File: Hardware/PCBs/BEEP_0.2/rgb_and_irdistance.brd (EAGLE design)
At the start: 22.2 x 13.3 mm, 5 parts, among them X1 MICROMATCH-8

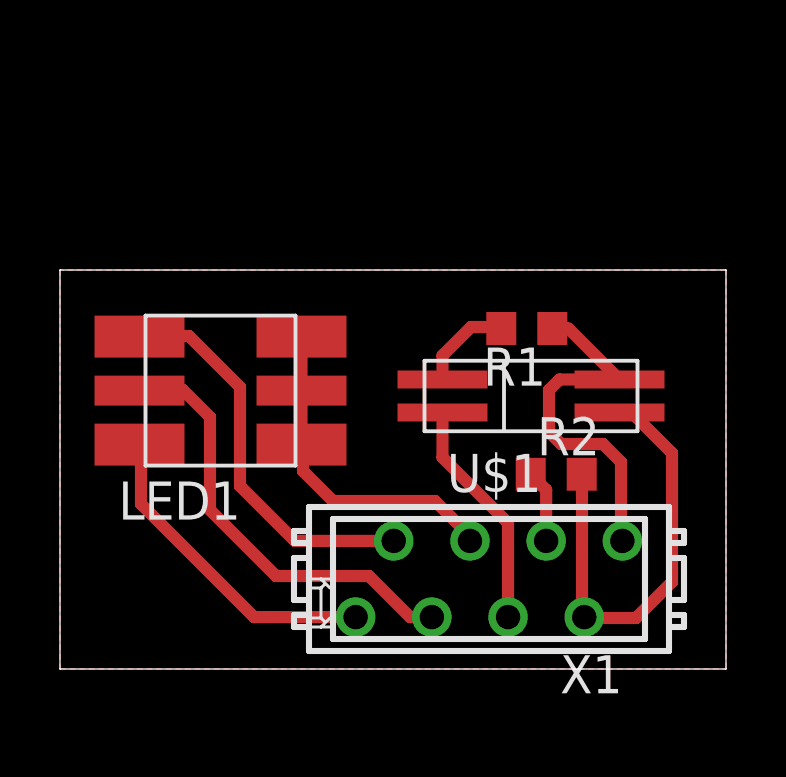
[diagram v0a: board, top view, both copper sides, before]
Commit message: enhance routing fix rgb and ir distance board (connector was on the wrong side)
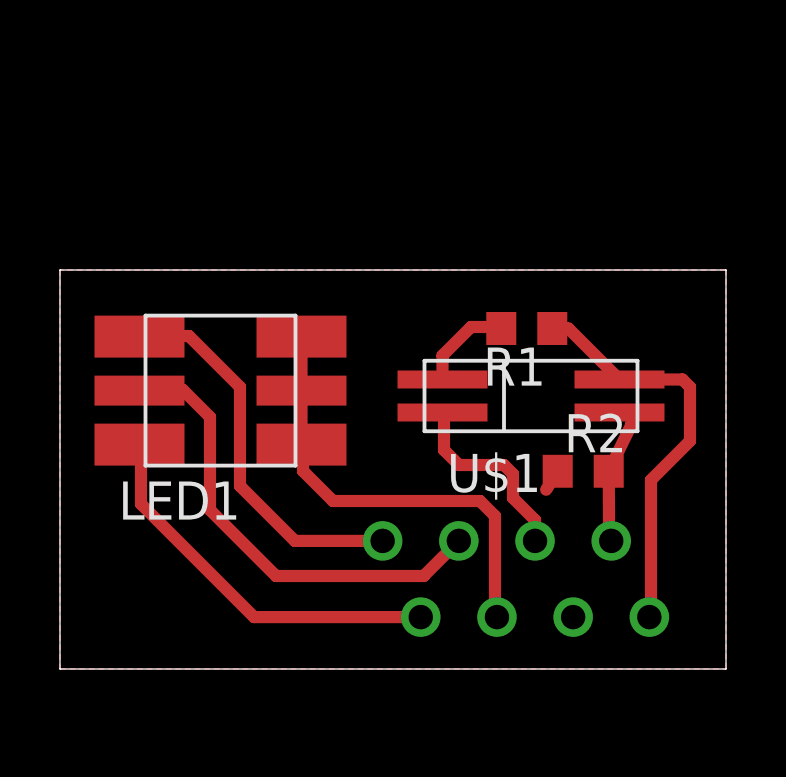
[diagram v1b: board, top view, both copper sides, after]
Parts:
- moved R2 0.91 mm to (17.4, 6.59)
- moved X1 0.90 mm to (15.2, 3.00), flipped to the bottom, turned to 0 degrees
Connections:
- net RGB_ANODE_1: now also LED1.R1; no longer LED1.B1
- net RGB_ANODE_3: now also LED1.B1; no longer LED1.R1
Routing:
- net ADISTANCE: track 14.9 -> 4.89 mm
- net RGB_COMMON_K: track 11.1 -> 14.9 mm
- net RGB_ANODE_1: track 10.8 -> 12.9 mm
- net GND: track 2.43 -> 0.73 mm
- net IR_LED_K: track 8.70 -> 7.41 mm
- net +5V: track 12.4 -> 13.6 mm
- net RGB_ANODE_2: track 14.7 -> 15.5 mm
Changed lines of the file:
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@@
 <element name="LED1" library="BEEP" package="5050LED" value="F503605050" x="5.35" y="9.28"/>
 <element name="R1" library="rcl" package="R0603" value="" x="15.56" y="11.35" rot="R180"/>
-<element name="R2" library="rcl" package="R0603" value="" x="16.54" y="6.49"/>
-<element name="X1" library="con-amp-micromatch" package="MICROMATCH-8" value="MICROMATCH-8" x="14.3" y="3" rot="R180">
-<attribute name="OC_NEWARK" value="26H0301" x="14.3" y="3" size="1.778" layer="27" rot="R180" display="off"/>
-<attribute name="MPN" value="7-215464-8" x="14.3" y="3" size="1.778" layer="27" rot="R180" display="off"/>
-<attribute name="MF" value="FARNELL" x="14.3" y="3" size="1.778" layer="27" rot="R180" display="off"/>
-<attribute name="OC_FARNELL" value="3784642" x="14.3" y="3" size="1.778" layer="27" rot="R180" display="off"/>
+<element name="R2" library="rcl" package="R0603" value="" x="17.44" y="6.59"/>
+<element name="X1" library="con-amp-micromatch" package="MICROMATCH-8" value="MICROMATCH-8" x="15.2" y="3" rot="MR0">
+<attribute name="OC_NEWARK" value="26H0301" x="15.2" y="3" size="1.778" layer="28" rot="MR0" display="off"/>
+<attribute name="MPN" value="7-215464-8" x="15.2" y="3" size="1.778" layer="28" rot="MR0" display="off"/>
+<attribute name="MF" value="FARNELL" x="15.2" y="3" size="1.778" layer="28" rot="MR0" display="off"/>
+<attribute name="OC_FARNELL" value="3784642" x="15.2" y="3" size="1.778" layer="28" rot="MR0" display="off"/>
 </element>
 <element name="U$1" library="BEEP" package="HSDL-9100" value="HSDL-9100" x="15.7" y="9.1"/>
@@
 <wire x1="8.05" y1="7.48" x2="8.05" y2="9.28" width="0.4064" layer="1"/>
 <wire x1="8.05" y1="9.28" x2="8.05" y2="11.08" width="0.4064" layer="1"/>
-<wire x1="13.665" y1="4.27" x2="13.665" y2="4.435" width="0.4064" layer="1"/>
-<wire x1="13.665" y1="4.435" x2="12.5" y2="5.6" width="0.4064" layer="1"/>
-<wire x1="12.5" y1="5.6" x2="9.1" y2="5.6" width="0.4064" layer="1"/>
 <wire x1="9.1" y1="5.6" x2="8.1" y2="6.6" width="0.4064" layer="1"/>
+<wire x1="9.1" y1="5.6" x2="14" y2="5.6" width="0.4064" layer="1"/>
+<wire x1="14" y1="5.6" x2="14.5" y2="5.1" width="0.4064" layer="1"/>
+<wire x1="14.5" y1="5.1" x2="14.5" y2="1.795" width="0.4064" layer="1"/>
+<wire x1="14.5" y1="1.795" x2="14.565" y2="1.73" width="0.4064" layer="1"/>
 </signal>
 <signal name="ADISTANCE">
@@
 <contactref element="U$1" pad="DET_A"/>
 <wire x1="18.65" y1="8.55" x2="19.05" y2="8.55" width="0.4064" layer="1"/>
-<wire x1="19.05" y1="8.55" x2="20.4" y2="7.2" width="0.4064" layer="1"/>
-<wire x1="20.4" y1="7.2" x2="20.4" y2="2.9" width="0.4064" layer="1"/>
-<wire x1="20.4" y1="2.9" x2="19.2" y2="1.7" width="0.4064" layer="1"/>
-<wire x1="19.2" y1="1.7" x2="17.545" y2="1.7" width="0.4064" layer="1"/>
-<wire x1="17.545" y1="1.7" x2="17.475" y2="1.73" width="0.4064" layer="1"/>
-<wire x1="17.4" y1="6.18" x2="17.4" y2="1.705" width="0.4064" layer="1"/>
-<wire x1="17.4" y1="1.705" x2="17.475" y2="1.73" width="0.4064" layer="1"/>
-<wire x1="17.4" y1="6.18" x2="17.39" y2="6.49" width="0.4064" layer="1"/>
+<wire x1="18.3" y1="5.28" x2="18.29" y2="6.59" width="0.4064" layer="1"/>
+<wire x1="18.3" y1="5.28" x2="18.3" y2="4.345" width="0.4064" layer="1"/>
+<wire x1="18.3" y1="4.345" x2="18.375" y2="4.27" width="0.4064" layer="1"/>
+<wire x1="19.05" y1="8.55" x2="19.05" y2="8.15" width="0.4064" layer="1"/>
+<wire x1="19.05" y1="8.15" x2="18.29" y2="6.59" width="0.4064" layer="1"/>
 </signal>
 <signal name="N$2">
@@
 </signal>
 <signal name="RGB_ANODE_1">
-<contactref element="LED1" pad="B1"/>
 <contactref element="X1" pad="1"/>
-<wire x1="2.6" y1="7.43" x2="2.65" y2="7.48" width="0.4064" layer="1"/>
-<wire x1="9.855" y1="1.73" x2="6.47" y2="1.73" width="0.4064" layer="1"/>
-<wire x1="6.47" y1="1.73" x2="2.7" y2="5.5" width="0.4064" layer="1"/>
-<wire x1="2.7" y1="5.5" x2="2.7" y2="7.43" width="0.4064" layer="1"/>
-<wire x1="2.7" y1="7.43" x2="2.65" y2="7.48" width="0.4064" layer="1"/>
+<contactref element="LED1" pad="R1"/>
+<wire x1="6" y1="9.4" x2="4.3" y2="11.1" width="0.4064" layer="1"/>
+<wire x1="4.3" y1="11.1" x2="2.67" y2="11.1" width="0.4064" layer="1"/>
+<wire x1="2.67" y1="11.1" x2="2.65" y2="11.08" width="0.4064" layer="1"/>
+<wire x1="7.83" y1="4.27" x2="6" y2="6.1" width="0.4064" layer="1"/>
+<wire x1="6" y1="6.1" x2="6" y2="9.4" width="0.4064" layer="1"/>
+<wire x1="7.83" y1="4.27" x2="10.755" y2="4.27" width="0.4064" layer="1"/>
 </signal>
 <signal name="RGB_ANODE_2">
@@
 <wire x1="2.67" y1="9.3" x2="2.65" y2="9.28" width="0.4064" layer="1"/>
 <contactref element="X1" pad="3"/>
-<wire x1="12.395" y1="1.73" x2="11.67" y2="1.73" width="0.4064" layer="1"/>
-<wire x1="11.67" y1="1.73" x2="10.3" y2="3.1" width="0.4064" layer="1"/>
-<wire x1="10.3" y1="3.1" x2="7.2" y2="3.1" width="0.4064" layer="1"/>
 <wire x1="7.2" y1="3.1" x2="5" y2="5.3" width="0.4064" layer="1"/>
+<wire x1="7.2" y1="3.1" x2="12.125" y2="3.1" width="0.4064" layer="1"/>
+<wire x1="12.125" y1="3.1" x2="13.295" y2="4.27" width="0.4064" layer="1"/>
 </signal>
 <signal name="RGB_ANODE_3">
-<contactref element="LED1" pad="R1"/>
-<wire x1="6" y1="9.4" x2="4.3" y2="11.1" width="0.4064" layer="1"/>
-<wire x1="4.3" y1="11.1" x2="2.67" y2="11.1" width="0.4064" layer="1"/>
-<wire x1="2.67" y1="11.1" x2="2.65" y2="11.08" width="0.4064" layer="1"/>
 <contactref element="X1" pad="2"/>
-<wire x1="11.125" y1="4.27" x2="7.83" y2="4.27" width="0.4064" layer="1"/>
-<wire x1="7.83" y1="4.27" x2="6" y2="6.1" width="0.4064" layer="1"/>
-<wire x1="6" y1="6.1" x2="6" y2="9.4" width="0.4064" layer="1"/>
+<contactref element="LED1" pad="B1"/>
+<wire x1="2.6" y1="7.43" x2="2.65" y2="7.48" width="0.4064" layer="1"/>
+<wire x1="6.47" y1="1.73" x2="2.7" y2="5.5" width="0.4064" layer="1"/>
+<wire x1="2.7" y1="5.5" x2="2.7" y2="7.43" width="0.4064" layer="1"/>
+<wire x1="2.7" y1="7.43" x2="2.65" y2="7.48" width="0.4064" layer="1"/>
+<wire x1="6.47" y1="1.73" x2="12.025" y2="1.73" width="0.4064" layer="1"/>
 </signal>
 <signal name="IR_LED_K">
 <contactref element="U$1" pad="LED_K"/>
 <contactref element="X1" pad="5"/>
-<wire x1="14.935" y1="1.73" x2="14.935" y2="4.865" width="0.4064" layer="1"/>
 <wire x1="11.8" y1="8.5" x2="12.7" y2="8.5" width="0.4064" layer="1"/>
 <wire x1="12.7" y1="8.5" x2="12.75" y2="8.55" width="0.4064" layer="1"/>
-<wire x1="14.935" y1="4.865" x2="12.75" y2="7.05" width="0.4064" layer="1"/>
-<wire x1="12.75" y1="8.55" x2="12.75" y2="7.05" width="0.4064" layer="1"/>
+<wire x1="15.835" y1="4.27" x2="15.835" y2="4.965" width="0.4064" layer="1"/>
+<wire x1="15.835" y1="4.965" x2="15.1" y2="5.7" width="0.4064" layer="1"/>
+<wire x1="15.1" y1="5.7" x2="15.1" y2="6.5" width="0.4064" layer="1"/>
+<wire x1="15.1" y1="6.5" x2="14.8" y2="6.8" width="0.4064" layer="1"/>
+<wire x1="14.8" y1="6.8" x2="13.3" y2="6.8" width="0.4064" layer="1"/>
+<wire x1="13.3" y1="6.8" x2="12.8" y2="7.3" width="0.4064" layer="1"/>
+<wire x1="12.8" y1="7.3" x2="12.8" y2="8.5" width="0.4064" layer="1"/>
+<wire x1="12.8" y1="8.5" x2="12.75" y2="8.55" width="0.4064" layer="1"/>
 </signal>
 <signal name="+5V">
@@
 <wire x1="16.41" y1="11.35" x2="16.95" y2="11.35" width="0.4064" layer="1"/>
 <wire x1="16.95" y1="11.35" x2="18.65" y2="9.65" width="0.4064" layer="1"/>
-<wire x1="18.65" y1="9.65" x2="16.65" y2="9.65" width="0.4064" layer="1"/>
-<wire x1="16.65" y1="9.65" x2="16.3" y2="9.3" width="0.4064" layer="1"/>
-<wire x1="16.3" y1="9.3" x2="16.3" y2="7.9" width="0.4064" layer="1"/>
-<wire x1="16.3" y1="7.9" x2="16.7" y2="7.5" width="0.4064" layer="1"/>
-<wire x1="16.7" y1="7.5" x2="18.1" y2="7.5" width="0.4064" layer="1"/>
-<wire x1="18.1" y1="7.5" x2="18.7" y2="6.9" width="0.4064" layer="1"/>
-<wire x1="18.7" y1="6.9" x2="18.7" y2="4.215" width="0.4064" layer="1"/>
-<wire x1="18.7" y1="4.215" x2="18.745" y2="4.27" width="0.4064" layer="1"/>
+<wire x1="18.65" y1="9.65" x2="20.75" y2="9.65" width="0.4064" layer="1"/>
+<wire x1="20.75" y1="9.65" x2="21" y2="9.4" width="0.4064" layer="1"/>
+<wire x1="21" y1="9.4" x2="21" y2="7.6" width="0.4064" layer="1"/>
+<wire x1="21" y1="7.6" x2="19.7" y2="6.3" width="0.4064" layer="1"/>
+<wire x1="19.7" y1="6.3" x2="19.7" y2="1.785" width="0.4064" layer="1"/>
+<wire x1="19.7" y1="1.785" x2="19.645" y2="1.73" width="0.4064" layer="1"/>
 </signal>
 <signal name="GND">
@@
 <vertex x="0" y="13.3"/>
 </polygon>
-<wire x1="16.205" y1="4.27" x2="16.205" y2="5.975" width="0.4064" layer="1"/>
-<wire x1="16.205" y1="5.975" x2="15.69" y2="6.49" width="0.4064" layer="1"/>
+<wire x1="16.205" y1="5.975" x2="16.59" y2="6.59" width="0.4064" layer="1"/>
 </signal>
 </signals>

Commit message: rearrange connectors routing
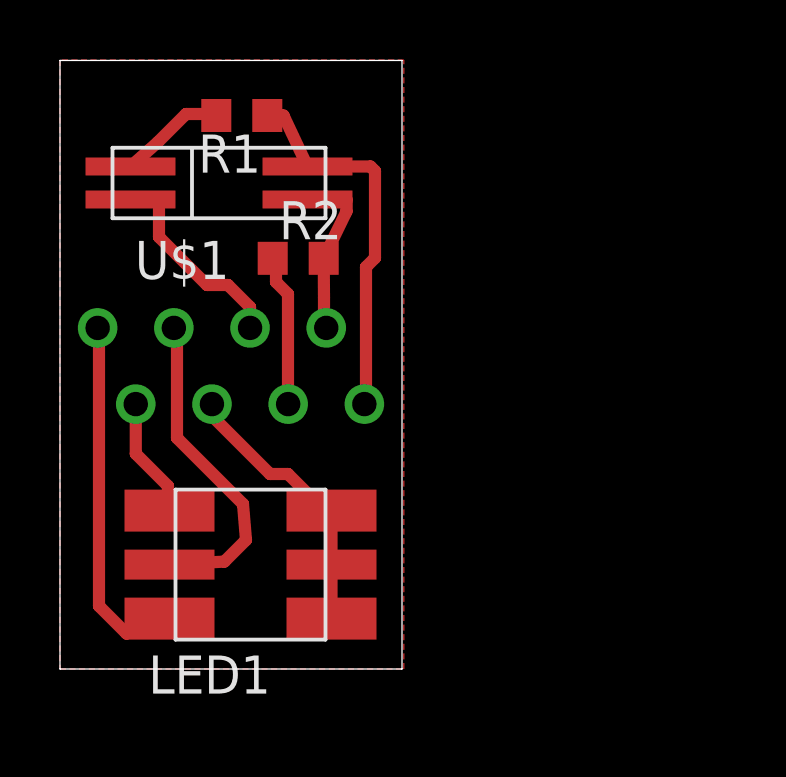
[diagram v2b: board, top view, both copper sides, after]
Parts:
- moved U$1 12.6 mm to (5.30, 16.2)
- moved R1 11.9 mm to (6.06, 18.4)
- moved R2 11.9 mm to (7.94, 13.7)
- moved X1 11.9 mm to (5.70, 10.1)
- moved LED1 5.89 mm to (6.35, 3.48)
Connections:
- net RGB_ANODE_1: now also LED1.B1; no longer LED1.R1
- net RGB_ANODE_3: now also LED1.R1; no longer LED1.B1
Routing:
- net RGB_ANODE_3: track 13.0 -> 4.70 mm
- net RGB_ANODE_2: track 15.5 -> 10.9 mm
- net GND: track 0.73 -> 5.14 mm
- net RGB_COMMON_K: track 14.9 -> 10.6 mm
- net IR_LED_K: track 7.41 -> 8.60 mm
- net +5V: track 13.6 -> 12.6 mm
- net ADISTANCE: track 4.89 -> 5.79 mm
- net RGB_ANODE_1: track 12.9 -> 12.1 mm
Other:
- board size 22.2 x 13.3 mm -> 11.4 x 20.3 mm

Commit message: move folders try to apply drc from sparkfun (wip) moved audio connetor add slice for camera flexcable
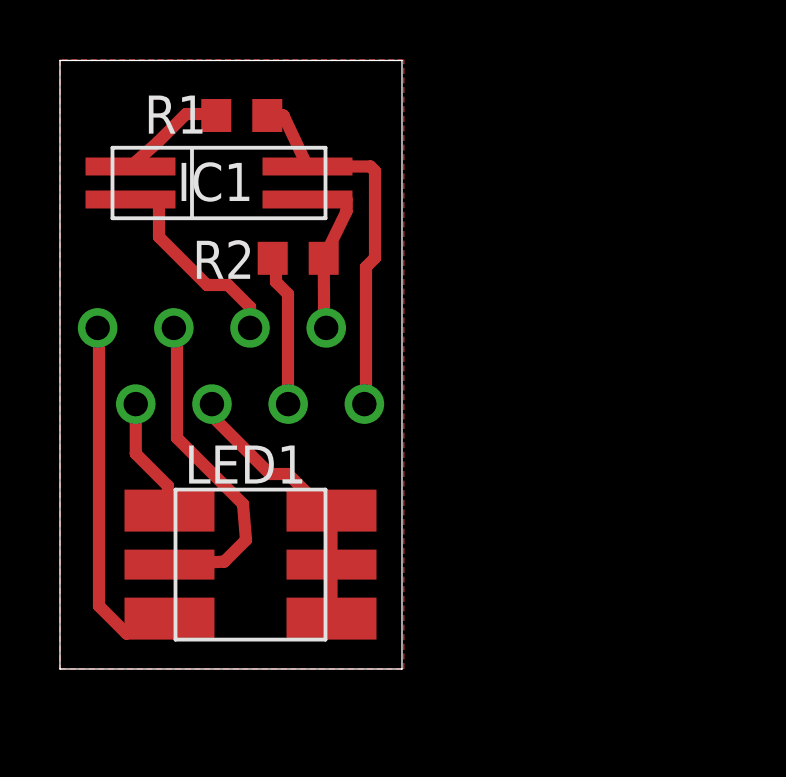
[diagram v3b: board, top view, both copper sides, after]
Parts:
- renumbered U$1 to IC1
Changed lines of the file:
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@@
 </autorouter>
 <elements>
-<element name="LED1" library="BEEP" package="5050LED" value="F503605050" x="6.35" y="3.48"/>
-<element name="R1" library="rcl" package="R0603" value="" x="6.06" y="18.45" rot="R180"/>
-<element name="R2" library="rcl" package="R0603" value="" x="7.94" y="13.69"/>
-<element name="X1" library="con-amp-micromatch" package="MICROMATCH-8" value="MICROMATCH-8" x="5.7" y="10.1" rot="MR0">
+<element name="LED1" library="BEEP" package="5050LED" value="F503605050" x="6.35" y="3.48" smashed="yes">
+<attribute name="NAME" x="4.15" y="6.18" size="1.27" layer="25"/>
+</element>
+<element name="R1" library="rcl" package="R0603" value="" x="6.06" y="18.45" smashed="yes" rot="R180">
+<attribute name="NAME" x="4.895" y="19.115" size="1.27" layer="25" rot="R180"/>
+<attribute name="VALUE" x="6.695" y="20.355" size="1.27" layer="27" rot="R180"/>
+</element>
+<element name="R2" library="rcl" package="R0603" value="" x="7.94" y="13.69" smashed="yes">
+<attribute name="NAME" x="6.495" y="14.275" size="1.27" layer="25" rot="R180"/>
+<attribute name="VALUE" x="7.305" y="11.785" size="1.27" layer="27"/>
+</element>
+<element name="X1" library="con-amp-micromatch" package="MICROMATCH-8" value="MICROMATCH-8" x="5.7" y="10.1" smashed="yes" rot="MR0">
 <attribute name="OC_NEWARK" value="26H0301" x="5.7" y="10.1" size="1.778" layer="28" rot="MR0" display="off"/>
 <attribute name="MPN" value="7-215464-8" x="5.7" y="10.1" size="1.778" layer="28" rot="MR0" display="off"/>
 <attribute name="MF" value="FARNELL" x="5.7" y="10.1" size="1.778" layer="28" rot="MR0" display="off"/>
 <attribute name="OC_FARNELL" value="3784642" x="5.7" y="10.1" size="1.778" layer="28" rot="MR0" display="off"/>
+<attribute name="NAME" x="3.145" y="12.74" size="1.27" layer="26" rot="MR0"/>
 </element>
-<element name="U$1" library="BEEP" package="HSDL-9100" value="HSDL-9100" x="5.3" y="16.2"/>
+<element name="IC1" library="BEEP" package="HSDL-9100" value="HSDL-9100" x="5.3" y="16.2" smashed="yes">
+<attribute name="NAME" x="3.9" y="15.6" size="1.27" layer="25"/>
+</element>
 </elements>
 <signals>
@@
 <contactref element="R2" pad="2"/>
 <contactref element="X1" pad="7"/>
-<contactref element="U$1" pad="DET_A"/>
+<contactref element="IC1" pad="DET_A"/>
 <wire x1="8.25" y1="15.65" x2="9.55" y2="15.65" width="0.4064" layer="1"/>
 <wire x1="8.8" y1="12.38" x2="8.79" y2="13.69" width="0.4064" layer="1"/>
@@
 <signal name="N$2">
 <contactref element="R1" pad="2"/>
-<contactref element="U$1" pad="LED_A"/>
+<contactref element="IC1" pad="LED_A"/>
 <wire x1="2.35" y1="16.75" x2="3.25" y2="17.55" width="0.4064" layer="1"/>
 <wire x1="3.25" y1="17.55" x2="4.2" y2="18.5" width="0.4064" layer="1"/>
@@
 </signal>
 <signal name="IR_LED_K">
-<contactref element="U$1" pad="LED_K"/>
+<contactref element="IC1" pad="LED_K"/>
 <contactref element="X1" pad="5"/>
 <wire x1="2.3" y1="15.6" x2="3.2" y2="15.6" width="0.4064" layer="1"/>
@@
 <signal name="+5V">
 <contactref element="R1" pad="1"/>
-<contactref element="U$1" pad="DET_K"/>
+<contactref element="IC1" pad="DET_K"/>
 <contactref element="X1" pad="8"/>
 <wire x1="6.91" y1="18.45" x2="7.45" y2="18.45" width="0.4064" layer="1"/>

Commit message: continue work on 3D model and replace connector for ir rgb board
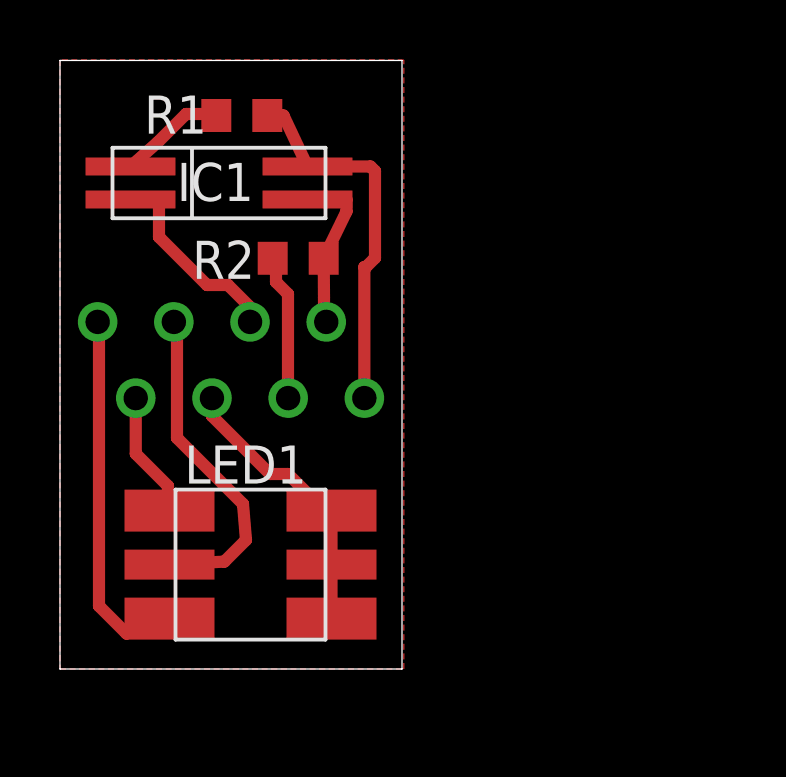
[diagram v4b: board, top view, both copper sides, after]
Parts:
- X1: value MICROMATCH-8 -> (none); device con-amp-micromatch:MICROMATCH-8 -> con-amp:FTOP-8
- moved X1 0.20 mm to (5.70, 10.3)
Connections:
- net +5V: now also X1.1; no longer X1.8
- net ADISTANCE: now also X1.2; no longer X1.7
- net GND: now also X1.3; no longer X1.6
- net IR_LED_K: now also X1.4; no longer X1.5
- net RGB_ANODE_1: now also X1.8; no longer X1.1
- net RGB_ANODE_2: now also X1.6; no longer X1.3
- net RGB_ANODE_3: now also X1.7; no longer X1.2
- net RGB_COMMON_K: now also X1.5; no longer X1.4

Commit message: modelling 3D model of case, minor change of ir / rgb board
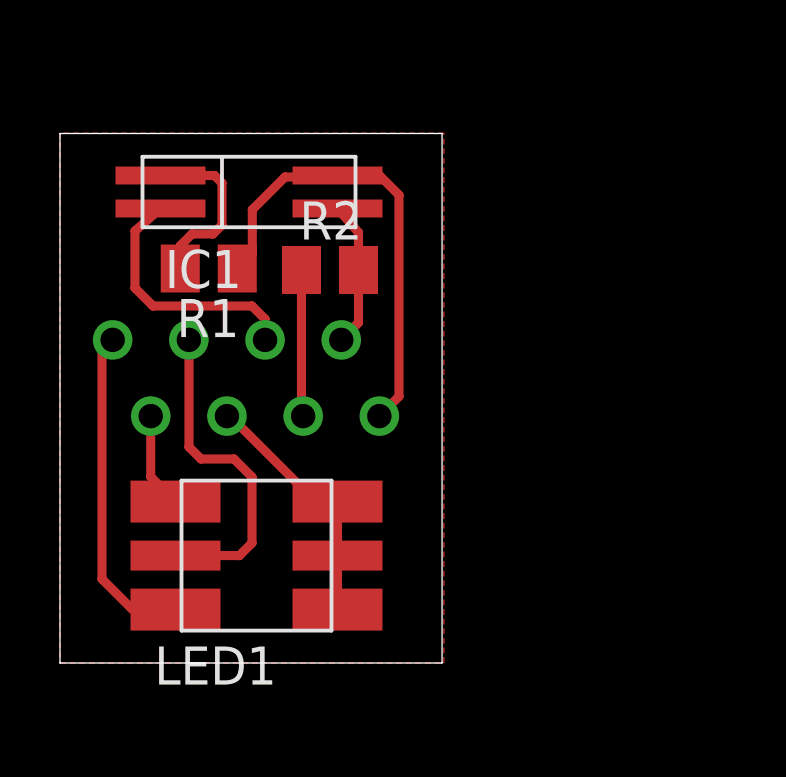
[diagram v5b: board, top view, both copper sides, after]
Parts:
- R1, R2: device rcl:R0603 -> resistor:M0805
- moved R1 5.22 mm to (4.96, 13.3)
- moved R2 1.13 mm to (9.00, 13.3)
- moved IC1 1.04 mm to (6.30, 15.9)
- moved X1 0.78 mm to (6.20, 9.70)
- moved LED1 0.36 mm to (6.55, 3.78)
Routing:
- net +5V: track 12.5 -> 15.4 mm
- net RGB_COMMON_K: track 10.8 -> 8.47 mm
- net N$2: track 3.87 -> 5.99 mm
- net RGB_ANODE_3: track 4.90 -> 3.19 mm
- net RGB_ANODE_1: track 12.3 -> 11.0 mm
- net ADISTANCE: track 5.88 -> 4.88 mm
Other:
- board size 11.4 x 20.3 mm -> 12.7 x 17.7 mm
